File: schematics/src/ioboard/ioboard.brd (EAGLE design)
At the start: 55.9 x 33.7 mm, 18 parts

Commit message: fixed headers
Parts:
- removed +12V, -12V, GND, JP2: (no value), pinhead:1X03
- added JP1, JP3: (no value), pinhead:2X03
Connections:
- net +12V: now also JP1.2, JP1.4, JP1.6; no longer +12V.1, +12V.2, +12V.3
- net -12V: now also JP3.1, JP3.3, JP3.5; no longer -12V.1, -12V.2, -12V.3
- net N$6: now also JP1.1, JP1.3, JP1.5; no longer JP2.1, JP2.2, JP2.3
- net N$9: now also JP3.2, JP3.4, JP3.6; no longer GND.1, GND.2, GND.3
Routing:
- net N$9: track 8.89 -> 9.42 mm
- net N$6: track 8.89 -> 9.42 mm
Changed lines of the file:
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@@
 <text x="53.975" y="17.145" size="1.4224" layer="25" font="vector" rot="R90">+12V</text>
 <text x="31.75" y="9.525" size="1.4224" layer="25" font="vector">+12V</text>
-<text x="4.445" y="10.795" size="1.27" layer="25" font="vector">GERB
+<text x="5.08" y="10.795" size="1.27" layer="25" font="vector">GERB
 STER
 2022</text>
@@
 <attribute name="VALUE" x="15.24" y="8.255" size="1.27" layer="27" ratio="10" rot="R270"/>
 </element>
-<element name="+12V" library="pinhead" library_urn="urn:adsk.eagle:library:325" package="1X03" package3d_urn="urn:adsk.eagle:package:22458/2" value="" x="53.34" y="26.67" smashed="yes" rot="R270">
-<attribute name="POPULARITY" value="92" x="53.34" y="26.67" size="1.778" layer="27" rot="R270" display="off"/>
-<attribute name="VALUE" x="50.165" y="30.48" size="1.27" layer="27" rot="R270"/>
-</element>
-<element name="JP2" library="pinhead" library_urn="urn:adsk.eagle:library:325" package="1X03" package3d_urn="urn:adsk.eagle:package:22458/2" value="" x="49.53" y="26.67" smashed="yes" rot="R90">
-<attribute name="POPULARITY" value="92" x="49.53" y="26.67" size="1.778" layer="27" rot="R90" display="off"/>
-<attribute name="VALUE" x="52.705" y="22.86" size="1.27" layer="27" rot="R90"/>
-</element>
-<element name="GND" library="pinhead" library_urn="urn:adsk.eagle:library:325" package="1X03" package3d_urn="urn:adsk.eagle:package:22458/2" value="" x="6.35" y="26.67" smashed="yes" rot="R90">
-<attribute name="POPULARITY" value="92" x="6.35" y="26.67" size="1.778" layer="27" rot="R90" display="off"/>
-<attribute name="VALUE" x="9.525" y="22.86" size="1.27" layer="27" rot="R90"/>
-</element>
-<element name="-12V" library="pinhead" library_urn="urn:adsk.eagle:library:325" package="1X03" package3d_urn="urn:adsk.eagle:package:22458/2" value="" x="2.54" y="26.67" smashed="yes" rot="R270">
-<attribute name="POPULARITY" value="92" x="2.54" y="26.67" size="1.778" layer="27" rot="R270" display="off"/>
-<attribute name="VALUE" x="-0.635" y="30.48" size="1.27" layer="27" rot="R270"/>
-</element>
 <element name="JP5" library="pinhead" library_urn="urn:adsk.eagle:library:325" package="1X04" package3d_urn="urn:adsk.eagle:package:22407/2" value="" x="38.1" y="15.875" smashed="yes" rot="R90">
 <attribute name="POPULARITY" value="91" x="38.1" y="15.875" size="1.778" layer="27" rot="R90" display="off"/>
@@
 <attribute name="POPULARITY" value="98" x="27.94" y="15.875" size="1.778" layer="27" display="off"/>
 <attribute name="VALUE" x="25.4" y="12.7" size="1.27" layer="27"/>
+</element>
+<element name="JP1" library="pinhead" library_urn="urn:adsk.eagle:library:325" package="2X03" package3d_urn="urn:adsk.eagle:package:22462/2" value="" x="52.07" y="26.67" smashed="yes" rot="R270">
+<attribute name="POPULARITY" value="62" x="52.07" y="26.67" size="1.778" layer="27" rot="R270" display="off"/>
+<attribute name="VALUE" x="47.625" y="30.48" size="1.27" layer="27" rot="R270"/>
+</element>
+<element name="JP3" library="pinhead" library_urn="urn:adsk.eagle:library:325" package="2X03" package3d_urn="urn:adsk.eagle:package:22462/2" value="" x="3.81" y="26.67" smashed="yes" rot="R270">
+<attribute name="POPULARITY" value="62" x="3.81" y="26.67" size="1.778" layer="27" rot="R270" display="off"/>
+<attribute name="VALUE" x="-0.635" y="30.48" size="1.27" layer="27" rot="R270"/>
 </element>
 </elements>
@@
 <contactref element="PWR" pad="10"/>
 <contactref element="POS_LED" pad="A"/>
-<contactref element="+12V" pad="3"/>
-<contactref element="+12V" pad="2"/>
-<contactref element="+12V" pad="1"/>
 <wire x1="33.02" y1="3.175" x2="33.02" y2="4.445" width="0.6096" layer="1"/>
 <wire x1="33.02" y1="4.445" x2="33.02" y2="5.715" width="0.6096" layer="1"/>
@@
 <wire x1="45.085" y1="6.985" x2="45.085" y2="8.255" width="0.6096" layer="1"/>
 <wire x1="45.085" y1="8.255" x2="53.34" y2="16.51" width="0.6096" layer="1"/>
+<contactref element="JP1" pad="2"/>
+<contactref element="JP1" pad="4"/>
+<contactref element="JP1" pad="6"/>
 <wire x1="53.34" y1="16.51" x2="53.34" y2="24.13" width="0.6096" layer="1"/>
-<wire x1="53.34" y1="29.21" x2="53.34" y2="24.13" width="0.6096" layer="1"/>
-<wire x1="53.34" y1="29.21" x2="53.34" y2="26.67" width="0" layer="19" extent="1-1"/>
+<wire x1="53.34" y1="24.13" x2="53.34" y2="26.67" width="0.6096" layer="1"/>
+<wire x1="53.34" y1="26.67" x2="53.34" y2="29.21" width="0.6096" layer="1"/>
 </signal>
 <signal name="-12V">
@@
 <contactref element="PWR" pad="2"/>
 <contactref element="R2" pad="2"/>
-<contactref element="-12V" pad="1"/>
-<contactref element="-12V" pad="2"/>
-<contactref element="-12V" pad="3"/>
-<wire x1="2.54" y1="29.21" x2="2.54" y2="26.67" width="0.6096" layer="1"/>
-<wire x1="2.54" y1="26.67" x2="2.54" y2="24.13" width="0.6096" layer="1"/>
-<wire x1="2.54" y1="24.13" x2="2.54" y2="16.51" width="0.6096" layer="1"/>
-<wire x1="2.54" y1="16.51" x2="9.525" y2="9.525" width="0.6096" layer="1"/>
+<wire x1="9.525" y1="9.525" x2="2.54" y2="16.51" width="0.6096" layer="1"/>
 <wire x1="9.525" y1="9.525" x2="15.24" y2="9.525" width="0.6096" layer="1"/>
 <wire x1="15.24" y1="9.525" x2="20.32" y2="4.445" width="0.6096" layer="1"/>
@@
 <wire x1="22.86" y1="4.445" x2="22.86" y2="5.715" width="0.6096" layer="1"/>
 <wire x1="22.86" y1="4.445" x2="22.86" y2="3.175" width="0.6096" layer="1"/>
+<contactref element="JP3" pad="1"/>
+<contactref element="JP3" pad="3"/>
+<contactref element="JP3" pad="5"/>
+<wire x1="2.54" y1="16.51" x2="2.54" y2="24.13" width="0.6096" layer="1"/>
+<wire x1="2.54" y1="29.21" x2="2.54" y2="26.67" width="0.6096" layer="1"/>
+<wire x1="2.54" y1="26.67" x2="2.54" y2="24.13" width="0.6096" layer="1"/>
 </signal>
 <signal name="N$1">
@@
 </signal>
 <signal name="N$6">
-<contactref element="JP2" pad="1"/>
-<contactref element="JP2" pad="2"/>
-<contactref element="JP2" pad="3"/>
 <contactref element="JP6" pad="1"/>
-<wire x1="49.53" y1="20.32" x2="49.53" y2="24.13" width="0.6096" layer="1"/>
-<wire x1="49.53" y1="24.13" x2="49.53" y2="26.67" width="0.6096" layer="1"/>
-<wire x1="49.53" y1="26.67" x2="49.53" y2="29.21" width="0.6096" layer="1"/>
+<contactref element="JP1" pad="1"/>
+<contactref element="JP1" pad="3"/>
+<contactref element="JP1" pad="5"/>
+<wire x1="49.53" y1="20.32" x2="49.53" y2="21.59" width="0.6096" layer="1"/>
+<wire x1="49.53" y1="21.59" x2="50.8" y2="22.86" width="0.6096" layer="1"/>
+<wire x1="50.8" y1="22.86" x2="50.8" y2="24.13" width="0.6096" layer="1"/>
+<wire x1="50.8" y1="29.21" x2="50.8" y2="26.67" width="0.6096" layer="1"/>
+<wire x1="50.8" y1="26.67" x2="50.8" y2="24.13" width="0.6096" layer="1"/>
 </signal>
 <signal name="N$9">
-<contactref element="GND" pad="1"/>
-<contactref element="GND" pad="2"/>
-<contactref element="GND" pad="3"/>
 <contactref element="GND_JMP" pad="1"/>
-<wire x1="6.35" y1="20.32" x2="6.35" y2="24.13" width="0.6096" layer="1"/>
-<wire x1="6.35" y1="24.13" x2="6.35" y2="26.67" width="0.6096" layer="1"/>
-<wire x1="6.35" y1="26.67" x2="6.35" y2="29.21" width="0.6096" layer="1"/>
+<contactref element="JP3" pad="2"/>
+<contactref element="JP3" pad="4"/>
+<contactref element="JP3" pad="6"/>
+<wire x1="5.08" y1="29.21" x2="5.08" y2="26.67" width="0.6096" layer="1"/>
+<wire x1="5.08" y1="26.67" x2="5.08" y2="24.13" width="0.6096" layer="1"/>
+<wire x1="5.08" y1="24.13" x2="5.08" y2="22.86" width="0.6096" layer="1"/>
+<wire x1="5.08" y1="22.86" x2="6.35" y2="21.59" width="0.6096" layer="1"/>
+<wire x1="6.35" y1="21.59" x2="6.35" y2="20.32" width="0.6096" layer="1"/>
 </signal>
 <signal name="N$3">

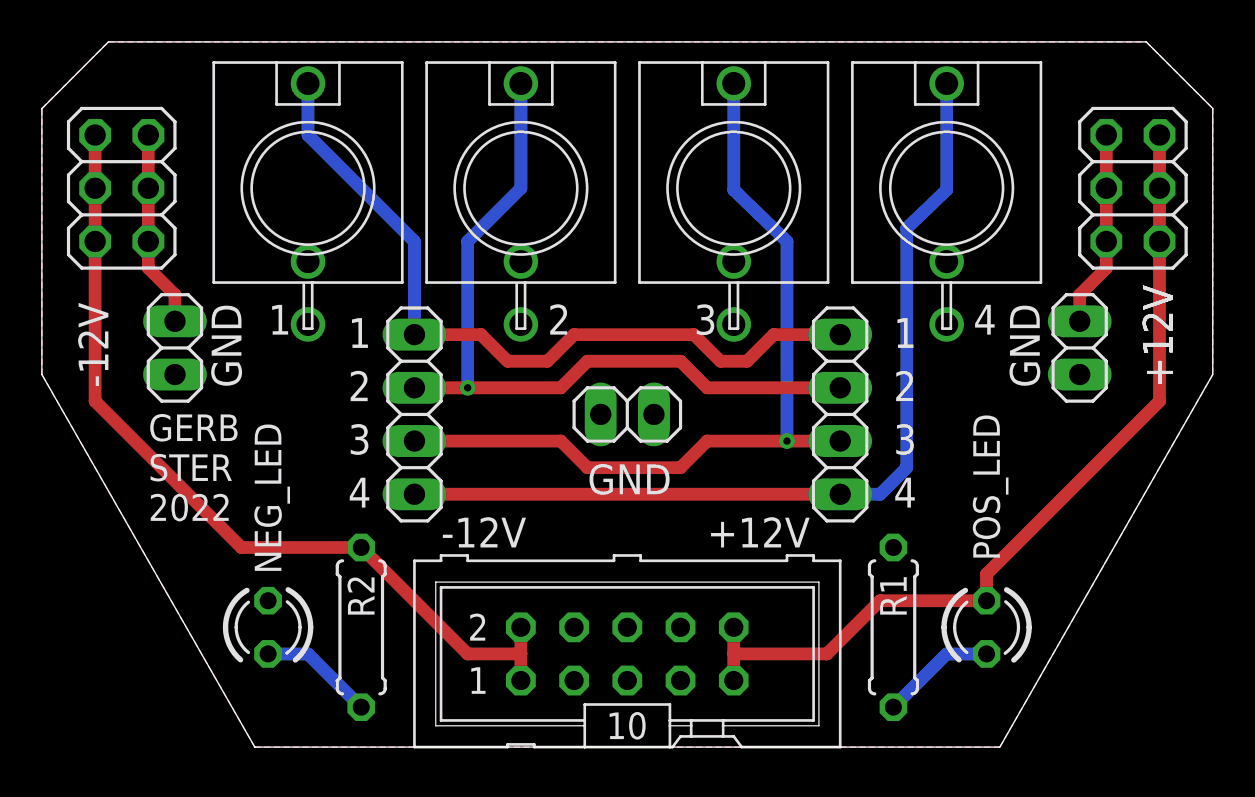
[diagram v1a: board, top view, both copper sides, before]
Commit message: Fixed schematics & descriptions
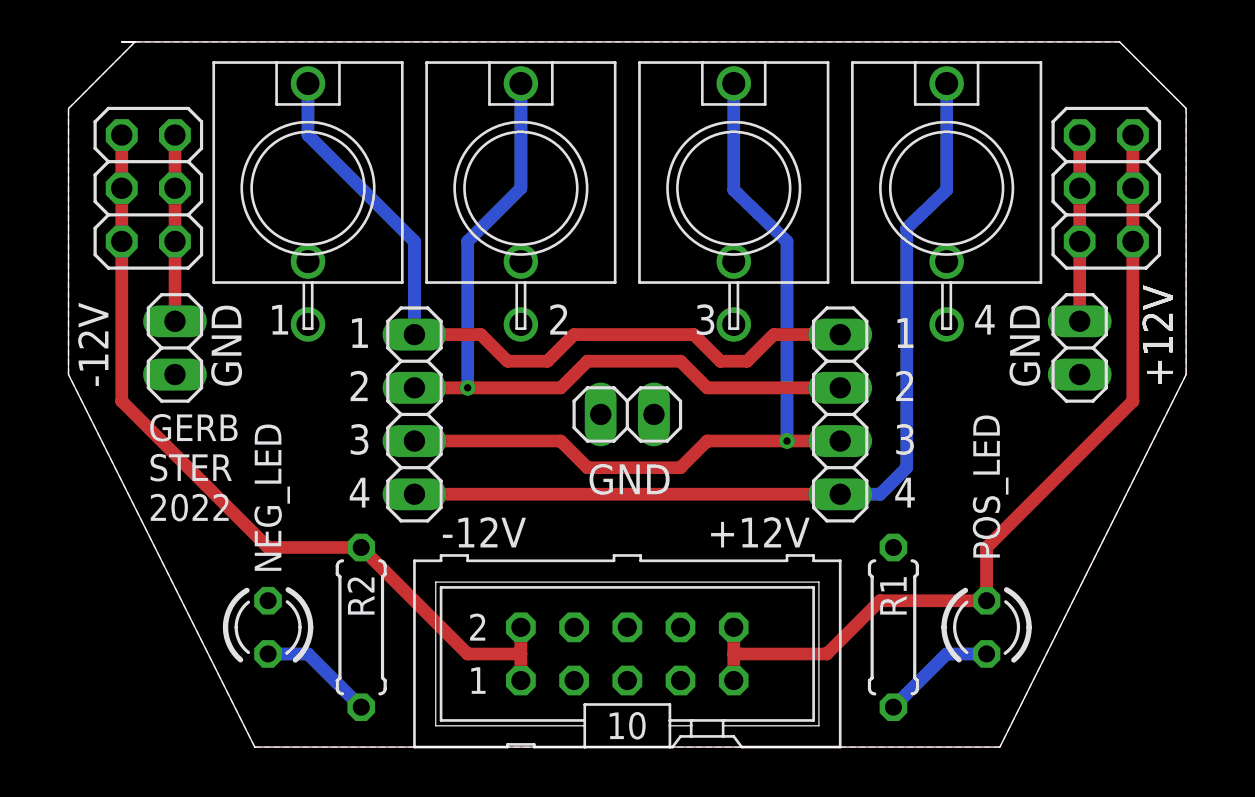
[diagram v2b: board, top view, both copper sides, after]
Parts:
- moved JP1 1.27 mm to (50.8, 26.7)
- moved JP3 1.27 mm to (5.08, 26.7)
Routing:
- net -12V: track 40.6 -> 39.3 mm
- net N$9: track 9.42 -> 8.89 mm
- net +12V: track 41.3 -> 40.8 mm
- net N$6: track 9.42 -> 8.89 mm
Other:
- board size 55.9 x 33.7 mm -> 53.3 x 33.7 mm
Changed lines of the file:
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@@
 <plain>
 <wire x1="10.16" y1="0" x2="45.72" y2="0" width="0" layer="20"/>
-<wire x1="45.72" y1="0" x2="55.88" y2="17.78" width="0" layer="20"/>
-<wire x1="55.88" y1="17.78" x2="55.88" y2="30.48" width="0" layer="20"/>
-<wire x1="55.88" y1="30.48" x2="52.705" y2="33.655" width="0" layer="20"/>
-<wire x1="52.705" y1="33.655" x2="3.175" y2="33.655" width="0" layer="20"/>
-<wire x1="3.175" y1="33.655" x2="3.165" y2="33.645" width="0" layer="20"/>
-<wire x1="3.165" y1="33.645" x2="0" y2="30.47" width="0" layer="20"/>
-<wire x1="0" y1="30.47" x2="0" y2="17.78" width="0" layer="20"/>
-<wire x1="0" y1="17.78" x2="10.16" y2="0" width="0" layer="20"/>
+<wire x1="45.72" y1="0" x2="54.61" y2="17.78" width="0" layer="20"/>
+<wire x1="54.61" y1="17.78" x2="54.61" y2="30.48" width="0" layer="20"/>
+<wire x1="54.61" y1="30.48" x2="51.435" y2="33.655" width="0" layer="20"/>
+<wire x1="51.435" y1="33.655" x2="3.81" y2="33.655" width="0" layer="20"/>
+<wire x1="3.81" y1="33.655" x2="4.435" y2="33.645" width="0" layer="20"/>
+<wire x1="4.435" y1="33.645" x2="1.27" y2="30.47" width="0" layer="20"/>
+<wire x1="1.27" y1="30.47" x2="1.27" y2="17.78" width="0" layer="20"/>
+<wire x1="1.27" y1="17.78" x2="10.16" y2="0" width="0" layer="20"/>
 <text x="53.975" y="17.145" size="1.4224" layer="25" font="vector" rot="R90">+12V</text>
 <text x="3.175" y="17.145" size="1.4224" layer="25" font="vector" rot="R90">-12V</text>
@@
 <attribute name="VALUE" x="25.4" y="12.7" size="1.27" layer="27"/>
 </element>
-<element name="JP1" library="pinhead" library_urn="urn:adsk.eagle:library:325" package="2X03" package3d_urn="urn:adsk.eagle:package:22462/2" value="" x="52.07" y="26.67" smashed="yes" rot="R270">
-<attribute name="POPULARITY" value="62" x="52.07" y="26.67" size="1.778" layer="27" rot="R270" display="off"/>
-<attribute name="VALUE" x="47.625" y="30.48" size="1.27" layer="27" rot="R270"/>
-</element>
-<element name="JP3" library="pinhead" library_urn="urn:adsk.eagle:library:325" package="2X03" package3d_urn="urn:adsk.eagle:package:22462/2" value="" x="3.81" y="26.67" smashed="yes" rot="R270">
-<attribute name="POPULARITY" value="62" x="3.81" y="26.67" size="1.778" layer="27" rot="R270" display="off"/>
-<attribute name="VALUE" x="-0.635" y="30.48" size="1.27" layer="27" rot="R270"/>
+<element name="JP1" library="pinhead" library_urn="urn:adsk.eagle:library:325" package="2X03" package3d_urn="urn:adsk.eagle:package:22462/2" value="" x="50.8" y="26.67" smashed="yes" rot="R270">
+<attribute name="POPULARITY" value="62" x="50.8" y="26.67" size="1.778" layer="27" rot="R270" display="off"/>
+<attribute name="VALUE" x="46.355" y="30.48" size="1.27" layer="27" rot="R270"/>
+</element>
+<element name="JP3" library="pinhead" library_urn="urn:adsk.eagle:library:325" package="2X03" package3d_urn="urn:adsk.eagle:package:22462/2" value="" x="5.08" y="26.67" smashed="yes" rot="R270">
+<attribute name="POPULARITY" value="62" x="5.08" y="26.67" size="1.778" layer="27" rot="R270" display="off"/>
+<attribute name="VALUE" x="0.635" y="30.48" size="1.27" layer="27" rot="R270"/>
 </element>
 </elements>
@@
 <contactref element="JP9" pad="1"/>
 <polygon width="0.4064" layer="16">
-<vertex x="0" y="17.78"/>
-<vertex x="0" y="30.48"/>
-<vertex x="3.175" y="33.655"/>
-<vertex x="52.705" y="33.655"/>
-<vertex x="55.88" y="30.48"/>
-<vertex x="55.88" y="17.78"/>
+<vertex x="1.27" y="17.78"/>
+<vertex x="1.27" y="30.48"/>
+<vertex x="4.445" y="33.655"/>
+<vertex x="51.435" y="33.655"/>
+<vertex x="54.61" y="30.48"/>
+<vertex x="54.61" y="17.78"/>
 <vertex x="45.72" y="0"/>
 <vertex x="10.16" y="0"/>
 </polygon>
 <polygon width="0.4064" layer="1">
-<vertex x="0" y="17.78"/>
-<vertex x="0" y="30.48"/>
-<vertex x="3.175" y="33.655"/>
-<vertex x="52.705" y="33.655"/>
-<vertex x="55.88" y="30.48"/>
-<vertex x="55.88" y="17.78"/>
+<vertex x="1.27" y="17.78"/>
+<vertex x="1.27" y="30.48"/>
+<vertex x="4.445" y="33.655"/>
+<vertex x="51.435" y="33.655"/>
+<vertex x="54.61" y="30.48"/>
+<vertex x="54.61" y="17.78"/>
 <vertex x="45.72" y="0"/>
 <vertex x="10.16" y="0"/>
@@
 <wire x1="40.005" y1="6.985" x2="37.465" y2="4.445" width="0.6096" layer="1"/>
 <wire x1="37.465" y1="4.445" x2="33.02" y2="4.445" width="0.6096" layer="1"/>
-<wire x1="45.085" y1="6.985" x2="45.085" y2="8.255" width="0.6096" layer="1"/>
-<wire x1="45.085" y1="8.255" x2="53.34" y2="16.51" width="0.6096" layer="1"/>
+<wire x1="45.085" y1="6.985" x2="45.085" y2="9.525" width="0.6096" layer="1"/>
+<wire x1="45.085" y1="9.525" x2="52.07" y2="16.51" width="0.6096" layer="1"/>
 <contactref element="JP1" pad="2"/>
 <contactref element="JP1" pad="4"/>
 <contactref element="JP1" pad="6"/>
-<wire x1="53.34" y1="16.51" x2="53.34" y2="24.13" width="0.6096" layer="1"/>
-<wire x1="53.34" y1="24.13" x2="53.34" y2="26.67" width="0.6096" layer="1"/>
-<wire x1="53.34" y1="26.67" x2="53.34" y2="29.21" width="0.6096" layer="1"/>
+<wire x1="52.07" y1="16.51" x2="52.07" y2="24.13" width="0.6096" layer="1"/>
+<wire x1="52.07" y1="24.13" x2="52.07" y2="26.67" width="0.6096" layer="1"/>
+<wire x1="52.07" y1="26.67" x2="52.07" y2="29.21" width="0.6096" layer="1"/>
 </signal>
 <signal name="-12V">
@@
 <contactref element="PWR" pad="2"/>
 <contactref element="R2" pad="2"/>
-<wire x1="9.525" y1="9.525" x2="2.54" y2="16.51" width="0.6096" layer="1"/>
-<wire x1="9.525" y1="9.525" x2="15.24" y2="9.525" width="0.6096" layer="1"/>
+<wire x1="10.795" y1="9.525" x2="3.81" y2="16.51" width="0.6096" layer="1"/>
+<wire x1="10.795" y1="9.525" x2="15.24" y2="9.525" width="0.6096" layer="1"/>
 <wire x1="15.24" y1="9.525" x2="20.32" y2="4.445" width="0.6096" layer="1"/>
 <wire x1="20.32" y1="4.445" x2="22.86" y2="4.445" width="0.6096" layer="1"/>
@@
 <contactref element="JP3" pad="3"/>
 <contactref element="JP3" pad="5"/>
-<wire x1="2.54" y1="16.51" x2="2.54" y2="24.13" width="0.6096" layer="1"/>
-<wire x1="2.54" y1="29.21" x2="2.54" y2="26.67" width="0.6096" layer="1"/>
-<wire x1="2.54" y1="26.67" x2="2.54" y2="24.13" width="0.6096" layer="1"/>
+<wire x1="3.81" y1="16.51" x2="3.81" y2="24.13" width="0.6096" layer="1"/>
+<wire x1="3.81" y1="29.21" x2="3.81" y2="26.67" width="0.6096" layer="1"/>
+<wire x1="3.81" y1="26.67" x2="3.81" y2="24.13" width="0.6096" layer="1"/>
 </signal>
 <signal name="N$1">
@@
 <contactref element="JP1" pad="3"/>
 <contactref element="JP1" pad="5"/>
-<wire x1="49.53" y1="20.32" x2="49.53" y2="21.59" width="0.6096" layer="1"/>
-<wire x1="49.53" y1="21.59" x2="50.8" y2="22.86" width="0.6096" layer="1"/>
-<wire x1="50.8" y1="22.86" x2="50.8" y2="24.13" width="0.6096" layer="1"/>
-<wire x1="50.8" y1="29.21" x2="50.8" y2="26.67" width="0.6096" layer="1"/>
-<wire x1="50.8" y1="26.67" x2="50.8" y2="24.13" width="0.6096" layer="1"/>
+<wire x1="49.53" y1="20.32" x2="49.53" y2="24.13" width="0.6096" layer="1"/>
+<wire x1="49.53" y1="29.21" x2="49.53" y2="26.67" width="0.6096" layer="1"/>
+<wire x1="49.53" y1="26.67" x2="49.53" y2="24.13" width="0.6096" layer="1"/>
 </signal>
 <signal name="N$9">
@@
 <contactref element="JP3" pad="4"/>
 <contactref element="JP3" pad="6"/>
-<wire x1="5.08" y1="29.21" x2="5.08" y2="26.67" width="0.6096" layer="1"/>
-<wire x1="5.08" y1="26.67" x2="5.08" y2="24.13" width="0.6096" layer="1"/>
-<wire x1="5.08" y1="24.13" x2="5.08" y2="22.86" width="0.6096" layer="1"/>
-<wire x1="5.08" y1="22.86" x2="6.35" y2="21.59" width="0.6096" layer="1"/>
-<wire x1="6.35" y1="21.59" x2="6.35" y2="20.32" width="0.6096" layer="1"/>
+<wire x1="6.35" y1="29.21" x2="6.35" y2="26.67" width="0.6096" layer="1"/>
+<wire x1="6.35" y1="26.67" x2="6.35" y2="24.13" width="0.6096" layer="1"/>
+<wire x1="6.35" y1="24.13" x2="6.35" y2="20.32" width="0.6096" layer="1"/>
 </signal>
 <signal name="N$3">
